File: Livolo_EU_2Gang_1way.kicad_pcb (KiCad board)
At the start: 2 copper layers, 43 x 43 mm, 51 parts, among them IC1 ATMEGA328P, U1 ATSHA204A, U2 RFM69CW, U3 MIC5205-3.3, U4 MCP16301, U5 AT25DF512C

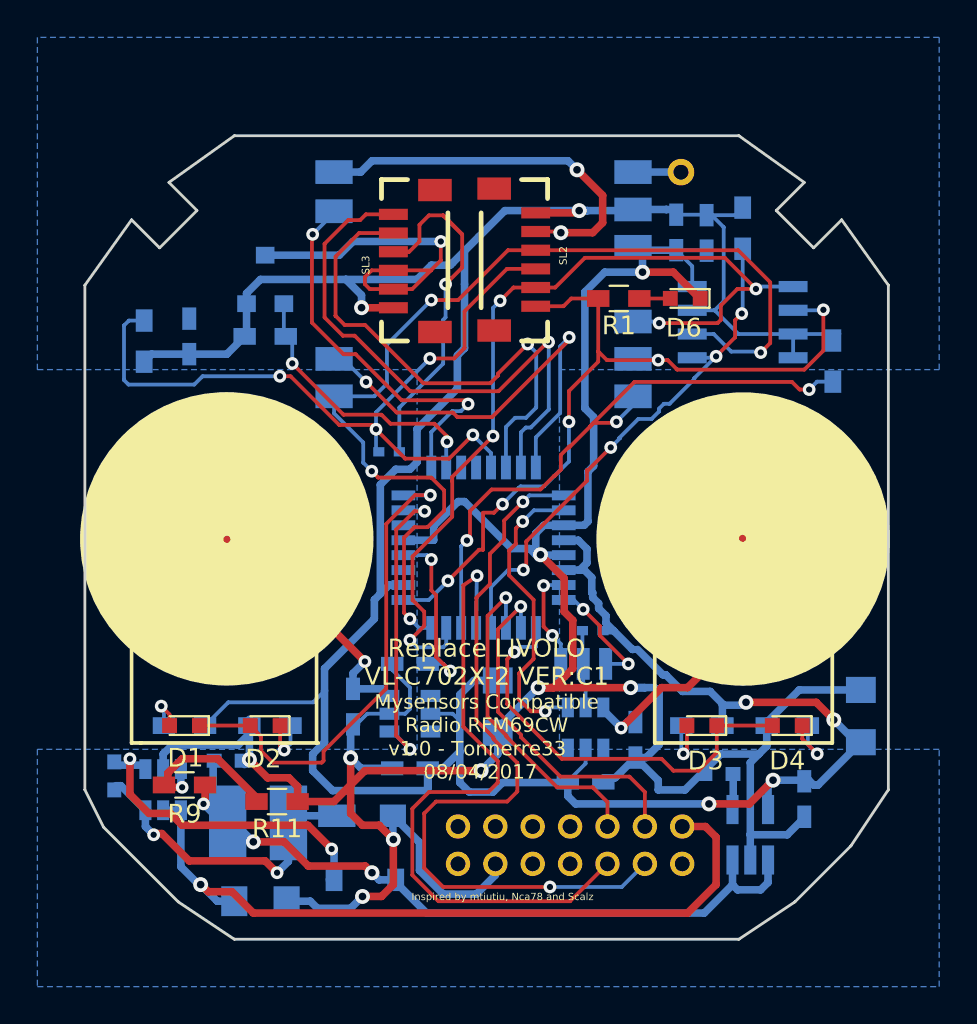
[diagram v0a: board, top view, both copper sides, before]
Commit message: Change RFM69 by NRF24L01 cause crash
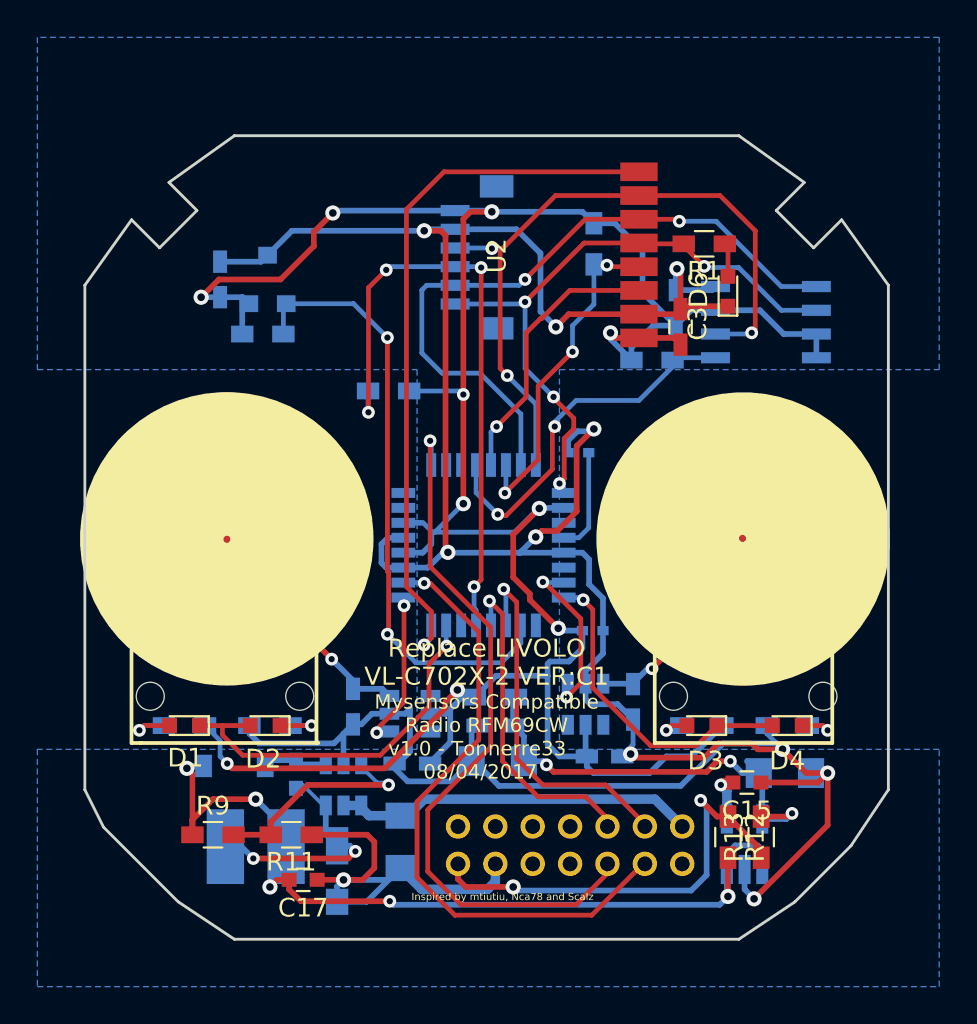
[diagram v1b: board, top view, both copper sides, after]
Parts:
- removed C1: 100n, Capacitors_SMD:C_0402
- removed SL3: ~, Livolo_EU_2Gang_1way:1X06-1MM
- removed U$3: 8MHZ, Livolo_EU_2Gang_1way:RESONATOR-SMD
- removed U$7: ANT, Livolo_EU_2Gang_1way:RFM12B-ANTENNA
- added L2: Ferrite_Bead, Resistors_SMD:R_0603_HandSoldering, B.Cu at (149.0, 113.5)
- added R12: *1, Resistors_SMD:R_0603_HandSoldering, F.Cu at (161.4, 121.0)
- added R13: *1, Resistors_SMD:R_0603_HandSoldering, F.Cu at (163.2, 121.0)
- added REF**: hole_1.5mm, Livolo:hole_1.5mm, F.Cu at (130.5, 113.5)
- added REF**: hole_1.5mm, Livolo:hole_1.5mm, F.Cu at (138.5, 113.5)
- added REF**: hole_1.5mm, Livolo:hole_1.5mm, F.Cu at (158.5, 113.5)
- added REF**: hole_1.5mm, Livolo:hole_1.5mm, F.Cu at (166.5, 113.5)
- C15, C17: moved to F.Cu
- C2: footprint Capacitors_SMD:C_0603_HandSoldering -> Capacitors_SMD:C_0402
- C3: value 10u -> 4.7u; moved to F.Cu
- SL2: moved to B.Cu
- U2: value RFM69CW -> NRF24L01; footprint Livolo_EU_2Gang_1way:RFM69CW_MINIMAL -> Livolo:NRF24L01-SMD; moved to F.Cu
- U5: footprint SOIC-8_3.9x4.9mm_Pitch1.27mm -> Housings_SOIC:SOIC-8_3.9x4.9mm_Pitch1.27mm
- moved C13 17.0 mm to (149.0, 115.1), turned to 180 degrees
- moved C2 14.5 mm to (153.4, 100.5)
- moved R4 14.2 mm to (154.2, 89.3)
- moved R2 13.4 mm to (143.3, 97.2), turned to 0 degrees
- moved C16 9.73 mm to (138.3, 117.7)
- moved U4 9.66 mm to (140.8, 118.2)
- moved D7 9.27 mm to (135.0, 117.2), turned to 180 degrees
- moved R10 8.57 mm to (157.4, 95.5), turned to 0 degrees
- moved C11 8.14 mm to (143.9, 121.3), turned to 90 degrees
- moved C17 7.53 mm to (138.7, 123.3)
- moved R1 5.43 mm to (160.1, 89.3)
- moved C12 5.08 mm to (164.5, 117.6), turned to 180 degrees
- moved C3 5.06 mm to (158.9, 93.7)
- moved C14 4.34 mm to (158.6, 92.7), turned to 90 degrees
- moved C5 3.47 mm to (134.2, 91.2)
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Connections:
- C10 pad +: VCC -> Net-(C10-Pad+)
- C12 pad +: VCC -> Net-(C10-Pad+)
- C13 pad 1: VCC -> Net-(C10-Pad+)
- C3 pad 1: VCC -> GND
- C3 pad 2: GND -> VCC
- IC1 pad 1: /L1_RST -> /TOUCH_L
- IC1 pad 10: /L2_SET -> (no net)
- IC1 pad 11: /L2_RST -> (no net)
- IC1 pad 13: /L1_SET -> /CE
- IC1 pad 2: /TOUCH_1 -> /L1_RST
- IC1 pad 23: /TOUCH_2 -> /TOUCH_R
- IC1 pad 24: /LED1 -> /LED2
- IC1 pad 25: /A2 -> (no net)
- IC1 pad 27: (no net) -> /L2_SET
- IC1 pad 28: (no net) -> /L2_RST
- IC1 pad 30: /D0_RX -> (no net)
- IC1 pad 31: /D1_TX -> /LED1
- IC1 pad 7: Net-(IC1-Pad7) -> (no net)
- IC1 pad 8: Net-(IC1-Pad8) -> (no net)
- IC1 pad 9: /LED2 -> /L1_SET
- U$2 pad 2: (no net) -> /3.3VCC-Liv
- U$4 pad 1: /TOUCH_1 -> /TOUCH_R
- U$6 pad 1: /TOUCH_2 -> /TOUCH_L
- U3 pad 5: VCC -> Net-(C10-Pad+)
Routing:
- net /D1_TX: track 30.5 -> 0.00 mm, vias 1 -> 0
- net VCC: track 174.9 -> 147.6 mm, vias 6 -> 10
- net /D0_RX: track 27.3 -> 0.00 mm, vias 1 -> 0
- net Net-(C10-Pad+): track 0.00 -> 25.6 mm, vias 0 -> 3
- net /3.3VCC-Liv: track 0.00 -> 23.6 mm, vias 0 -> 2
- net /A2: track 21.2 -> 0.00 mm, vias 2 -> 0
- net /+12VCC: track 41.0 -> 20.5 mm, vias 1 -> 0
- net /DTR: track 19.9 -> 0.00 mm, vias 1 -> 0
- net /A3_ATSHA: track 15.0 -> 32.9 mm
- net /MISO: track 55.3 -> 37.9 mm, vias 4 -> 3
- net /TOUCH_2: track 16.7 -> 0.00 mm, vias 2 -> 0
- net /TOUCH_1: track 16.1 -> 0.00 mm, vias 2 -> 0
- net /IRQ: track 23.4 -> 38.5 mm, vias 2 -> 1
- net /CE: track 0.00 -> 14.8 mm, vias 0 -> 1
- net /CSN: track 32.9 -> 18.2 mm
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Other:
- net class Default: clearance 0.2032 -> 0.3048; trace_width 0.2032 -> 0.254
- net class Power: clearance 0.254 -> 0.3048; trace_width 0.4064 -> 0.3048; via_dia 0.8 -> 0.8128
- rule trace_clearance: 0.2032 -> 0.3048

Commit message: Sketch test
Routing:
- net GND: track 189.6 -> 179.5 mm, vias 11 -> 10
- net /A3_ATSHA: track 32.9 -> 33.5 mm
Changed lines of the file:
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@@
     (thickness 1.6)
     (drawings 34)
-    (tracks 624)
+    (tracks 623)
     (zones 0)
     (modules 54)
@@
     (effects (font (size 0.38608 0.38608) (thickness 0.032512)) (justify bottom))
   )
+  (segment (start 154.728 109.99) (end 154.728 108.8255) (width 0.3048) (layer Bottom) (net 1))
+  (segment (start 153.62428 105.81678) (end 152.62606 105.81678) (width 0.3048) (layer Bottom) (net 1) (status 20))
+  (segment (start 153.9875 106.18) (end 153.62428 105.81678) (width 0.3048) (layer Bottom) (net 1))
+  (segment (start 153.9875 107.5135) (end 153.9875 106.18) (width 0.3048) (layer Bottom) (net 1))
+  (segment (start 154.4955 108.0215) (end 153.9875 107.5135) (width 0.3048) (layer Bottom) (net 1))
+  (segment (start 154.4955 108.593) (end 154.4955 108.0215) (width 0.3048) (layer Bottom) (net 1))
+  (segment (start 154.728 108.8255) (end 154.4955 108.593) (width 0.3048) (layer Bottom) (net 1))
   (segment (start 153.32075 103.60825) (end 153.32075 100.11575) (width 0.3048) (layer Top) (net 1))
   (segment (start 152.866 99.8085) (end 152.866 100.465) (width 0.3048) (layer Bottom) (net 1) (status 20))
@@
   (segment (start 150.241 105.81678) (end 146.57578 105.81678) (width 0.3048) (layer Bottom) (net 1))
   (segment (start 146.57578 105.81678) (end 146.3675 105.6085) (width 0.3048) (layer Bottom) (net 1))
-  (segment (start 154.728 109.99) (end 154.728 108.254) (width 0.3048) (layer Bottom) (net 1) (status 10))
-  (segment (start 154.728 108.254) (end 153.9875 107.5135) (width 0.3048) (layer Bottom) (net 1))
-  (segment (start 153.9875 107.5135) (end 153.9875 106.18) (width 0.3048) (layer Bottom) (net 1))
-  (segment (start 153.9875 106.18) (end 153.62428 105.81678) (width 0.3048) (layer Bottom) (net 1))
-  (segment (start 153.62428 105.81678) (end 152.62606 105.81678) (width 0.3048) (layer Bottom) (net 1) (status 20))
   (segment (start 153.797 112.827) (end 153.797 112.149) (width 0.3048) (layer Bottom) (net 1) (status 10))
   (segment (start 153.797 112.149) (end 154.728 111.218) (width 0.3048) (layer Bottom) (net 1))
@@
   (segment (start 145.35912 106.61688) (end 144.0434 106.61688) (width 0.3048) (layer Bottom) (net 1) (status 20))
   (segment (start 146.3675 105.6085) (end 145.35912 106.61688) (width 0.3048) (layer Bottom) (net 1))
-  (segment (start 162.306 122.77) (end 162.306 123.833) (width 0.3048) (layer Bottom) (net 1) (status 10))
-  (segment (start 166.751 120.404) (end 166.751 117.61) (width 0.3048) (layer Top) (net 1))
-  (segment (start 162.814 124.341) (end 166.751 120.404) (width 0.3048) (layer Top) (net 1))
-  (via (at 162.814 124.341) (size 0.8128) (drill 0.4064) (layers Top Bottom) (net 1))
-  (segment (start 162.306 123.833) (end 162.814 124.341) (width 0.3048) (layer Bottom) (net 1))
   (segment (start 140.843 117.145) (end 140.843 115.512) (width 0.3048) (layer Bottom) (net 1) (status 10))
   (segment (start 140.843 115.512) (end 141.351 115.004) (width 0.3048) (layer Bottom) (net 1) (status 20))
@@
   (segment (start 152.62606 108.21708) (end 153.54808 108.21708) (width 0.254) (layer Bottom) (net 5) (status 10))
   (via (at 153.67 108.339) (size 0.6858) (drill 0.3302) (layers Top Bottom) (net 5))
-  (segment (start 153.67 108.339) (end 154.178 108.847) (width 0.254) (layer Top) (net 5))
+  (segment (start 153.67 108.339) (end 154.1145 108.7835) (width 0.254) (layer Top) (net 5))
   (segment (start 159.7405 116.1495) (end 160.82 115.07) (width 0.254) (layer Top) (net 5) (status 20))
-  (segment (start 154.178 108.847) (end 154.178 113.038) (width 0.254) (layer Top) (net 5))
-  (segment (start 154.178 113.038) (end 157.2895 116.1495) (width 0.254) (layer Top) (net 5))
+  (segment (start 154.1145 108.7835) (end 154.1145 112.9745) (width 0.254) (layer Top) (net 5))
+  (segment (start 154.1145 112.9745) (end 157.2895 116.1495) (width 0.254) (layer Top) (net 5))
   (segment (start 157.2895 116.1495) (end 159.7405 116.1495) (width 0.254) (layer Top) (net 5))
   (segment (start 163.792 115.07) (end 160.82 115.07) (width 0.254) (layer Top) (net 5) (status 30))
@@
   (segment (start 159.047 89.289) (end 156.7 89.289) (width 0.254) (layer Top) (net 14) (status 30))
   (segment (start 156.7 89.289) (end 156.655 89.244) (width 0.254) (layer Top) (net 14) (status 30))
-  (segment (start 150.33498 109.70806) (end 150.33498 110.65802) (width 0.254) (layer Bottom) (net 15) (status 10))
-  (segment (start 141.37894 92.49194) (end 137.77722 92.49194) (width 0.254) (layer Bottom) (net 15) (status 20))
-  (segment (start 143.1925 94.3055) (end 141.37894 92.49194) (width 0.254) (layer Bottom) (net 15))
-  (via (at 143.1925 94.3055) (size 0.6858) (drill 0.3302) (layers Top Bottom) (net 15))
-  (segment (start 143.1925 106.815) (end 143.1925 94.3055) (width 0.254) (layer Top) (net 15))
-  (segment (start 143.256 106.8785) (end 143.1925 106.815) (width 0.254) (layer Top) (net 15))
-  (segment (start 143.256 110.117) (end 143.256 106.8785) (width 0.254) (layer Top) (net 15))
-  (segment (start 143.1925 110.1805) (end 143.256 110.117) (width 0.254) (layer Top) (net 15))
+  (segment (start 137.77722 92.49194) (end 141.56944 92.49194) (width 0.254) (layer Bottom) (net 15))
+  (segment (start 143.649698 94.572198) (end 143.649698 97.2265) (width 0.254) (layer Top) (net 15))
+  (segment (start 143.0655 93.988) (end 143.649698 94.572198) (width 0.254) (layer Top) (net 15))
+  (via (at 143.0655 93.988) (size 0.6858) (drill 0.3302) (layers Top Bottom) (net 15))
+  (segment (start 141.56944 92.49194) (end 143.0655 93.988) (width 0.254) (layer Bottom) (net 15))
+  (segment (start 150.33498 110.65802) (end 149.2885 111.7045) (width 0.254) (layer Bottom) (net 15))
+  (segment (start 143.649698 97.2265) (end 143.649698 107.754802) (width 0.254) (layer Top) (net 15))
+  (segment (start 143.649698 107.754802) (end 143.1925 108.212) (width 0.254) (layer Top) (net 15))
+  (segment (start 143.1925 108.212) (end 143.1925 110.1805) (width 0.254) (layer Top) (net 15))
+  (segment (start 150.33498 110.65802) (end 150.33498 109.70806) (width 0.254) (layer Bottom) (net 15) (status 10))
   (via (at 143.1925 110.1805) (size 0.6858) (drill 0.3302) (layers Top Bottom) (net 15))
   (segment (start 144.7165 111.7045) (end 143.1925 110.1805) (width 0.254) (layer Bottom) (net 15))
   (segment (start 149.2885 111.7045) (end 144.7165 111.7045) (width 0.254) (layer Bottom) (net 15))
-  (segment (start 150.33498 110.65802) (end 149.2885 111.7045) (width 0.254) (layer Bottom) (net 15))
+  (segment (start 143.649698 97.112198) (end 143.649698 97.2265) (width 0.254) (layer Top) (net 15))
   (segment (start 137.625 94.115) (end 137.625 92.64416) (width 0.254) (layer Bottom) (net 15) (status 30))
   (segment (start 137.625 92.64416) (end 137.77722 92.49194) (width 0.254) (layer Bottom) (net 15) (status 30))

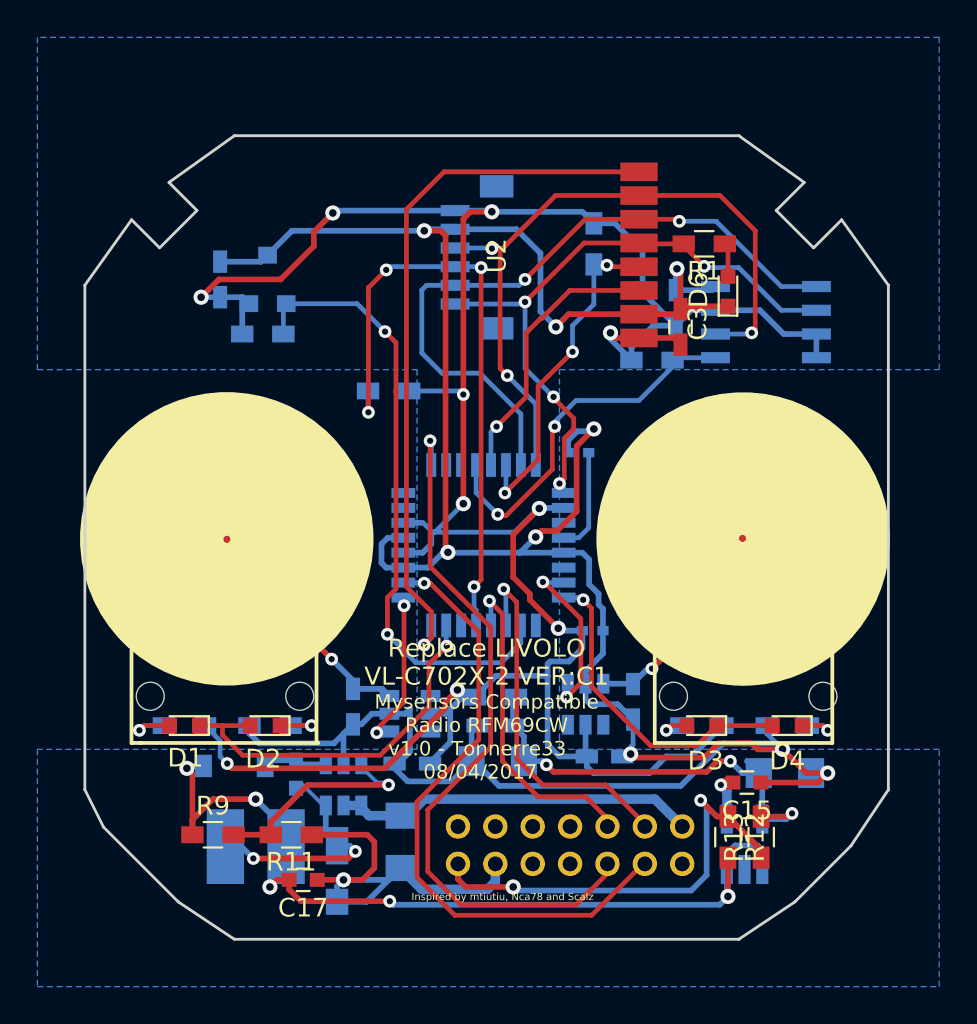
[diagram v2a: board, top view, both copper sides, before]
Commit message: update sketch and adding TTP223 documentation
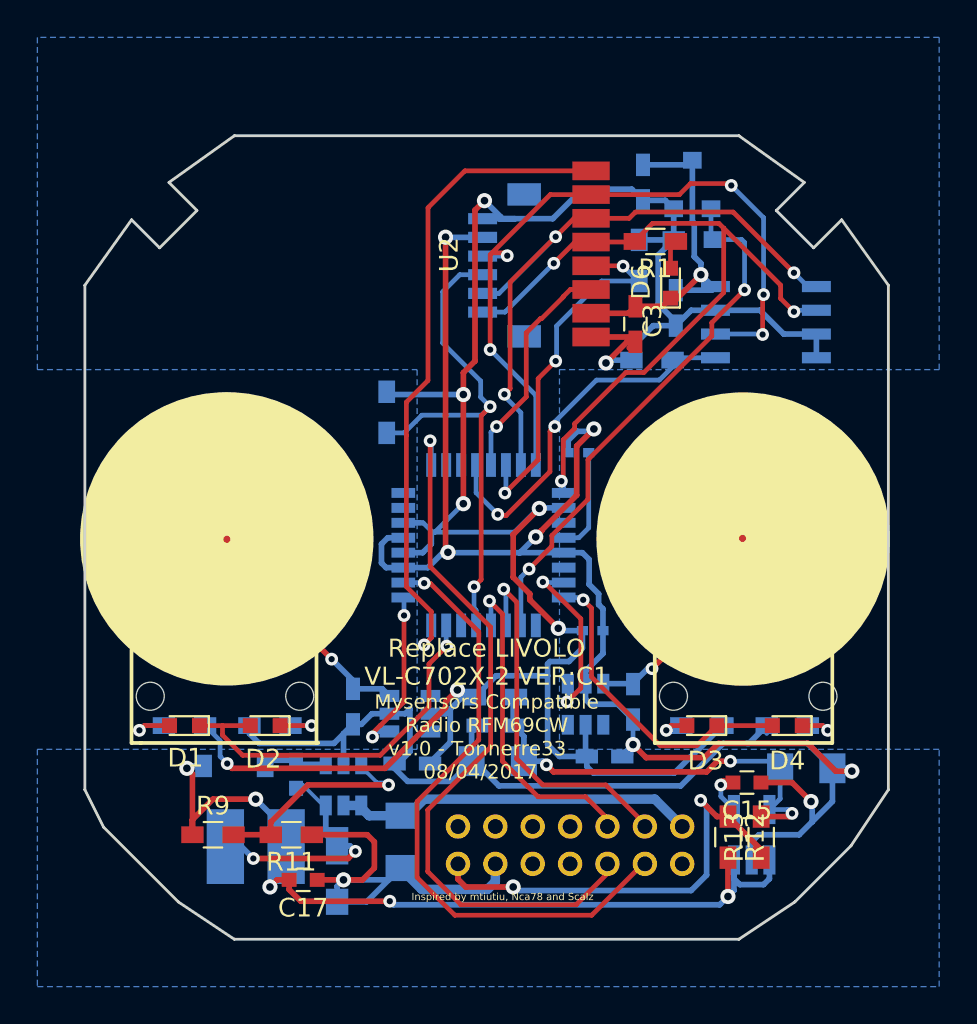
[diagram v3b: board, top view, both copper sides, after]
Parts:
- moved R3 23.6 mm to (159.6, 89.1)
- moved U1 23.3 mm to (159.5, 86.1)
- moved C5 23.2 mm to (156.9, 86.0)
- moved D6 3.10 mm to (158.3, 91.4)
- moved R1 2.62 mm to (157.5, 89.2)
- moved R4 2.58 mm to (156.7, 90.2)
- moved U2 2.57 mm to (145.4, 89.9)
- moved C3 2.42 mm to (156.5, 93.6)
- moved SL2 1.54 mm to (149.6, 90.5)
- moved C12 1.17 mm to (165.6, 117.4)
- moved R2 1.15 mm to (143.2, 98.3), turned to 90 degrees
- moved U3 0.63 mm to (162.7, 120.9)
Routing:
- net VCC: track 147.6 -> 135.7 mm, vias 10 -> 8
- net /SCK: track 33.9 -> 40.6 mm, vias 4 -> 3
- net /RST: track 33.7 -> 27.9 mm, vias 4 -> 2
- net /A3_ATSHA: track 33.5 -> 28.8 mm
- net GND: track 179.5 -> 174.9 mm, vias 10 -> 9
- net /IRQ: track 38.5 -> 35.3 mm
- net /MISO: track 37.9 -> 40.5 mm, vias 3 -> 5
- net /CE: track 14.8 -> 12.3 mm
- net /CSN: track 18.2 -> 20.4 mm
- net /MOSI: track 36.9 -> 35.0 mm, vias 2 -> 3
- net Net-(C10-Pad+): track 25.6 -> 24.5 mm
- net /TOUCH_L: track 8.92 -> 9.63 mm
- net /3.3VCC_1: track 48.4 -> 49.1 mm
